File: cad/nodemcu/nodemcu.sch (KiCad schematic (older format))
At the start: 1 part, among them P1 CONN_02X15

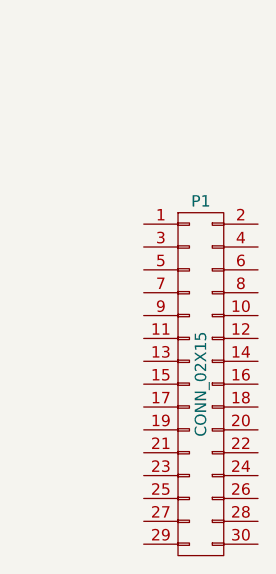
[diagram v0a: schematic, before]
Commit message: added schematic for nodemcu
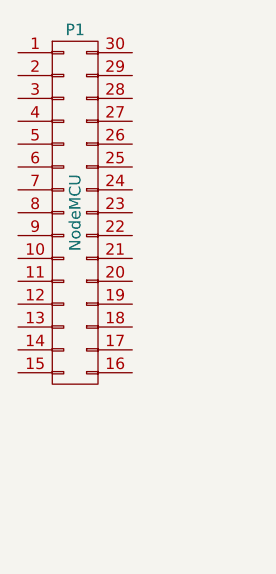
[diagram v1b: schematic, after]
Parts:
- removed P1: CONN_02X15, Housings_DIP:DIP-40_W25.4mm, symbol CONN_02X15
- added P1: NodeMCU, nodemcu:NodeMCU, symbol NodeMCU
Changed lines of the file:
@@
 LIBS:contrib
 LIBS:valves
+LIBS:nodemcu
+LIBS:nodemcu-cache
 EELAYER 25 0
 EELAYER END
@@
 $EndDescr
 $Comp
-L CONN_02X15 P1
-U 1 1 5777916F
-P 6150 3600
-F 0 "P1" H 6150 4400 50  0000 C CNN
-F 1 "CONN_02X15" V 6150 3600 50  0000 C CNN
-F 2 "Housings_DIP:DIP-40_W25.4mm" H 6150 2450 50  0001 C CNN
-F 3 "" H 6150 2450 50  0000 C CNN
-	1    6150 3600
+L NodeMCU P1
+U 1 1 5778EFB0
+P 5600 2850
+F 0 "P1" H 5600 3650 50  0000 C CNN
+F 1 "NodeMCU" V 5600 2850 50  0000 C CNN
+F 2 "nodemcu:NodeMCU" H 5600 1700 50  0001 C CNN
+F 3 "" H 5600 1700 50  0000 C CNN
+	1    5600 2850
 	1    0    0    -1
 $EndComp
